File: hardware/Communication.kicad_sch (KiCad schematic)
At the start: 28 parts, among them J16 Conn_01x04_Pin, J17 Conn_01x03_Male, J18 USB_C_Receptacle_USB2.0, U31 TXB0102DCT, U32 ADUM4160

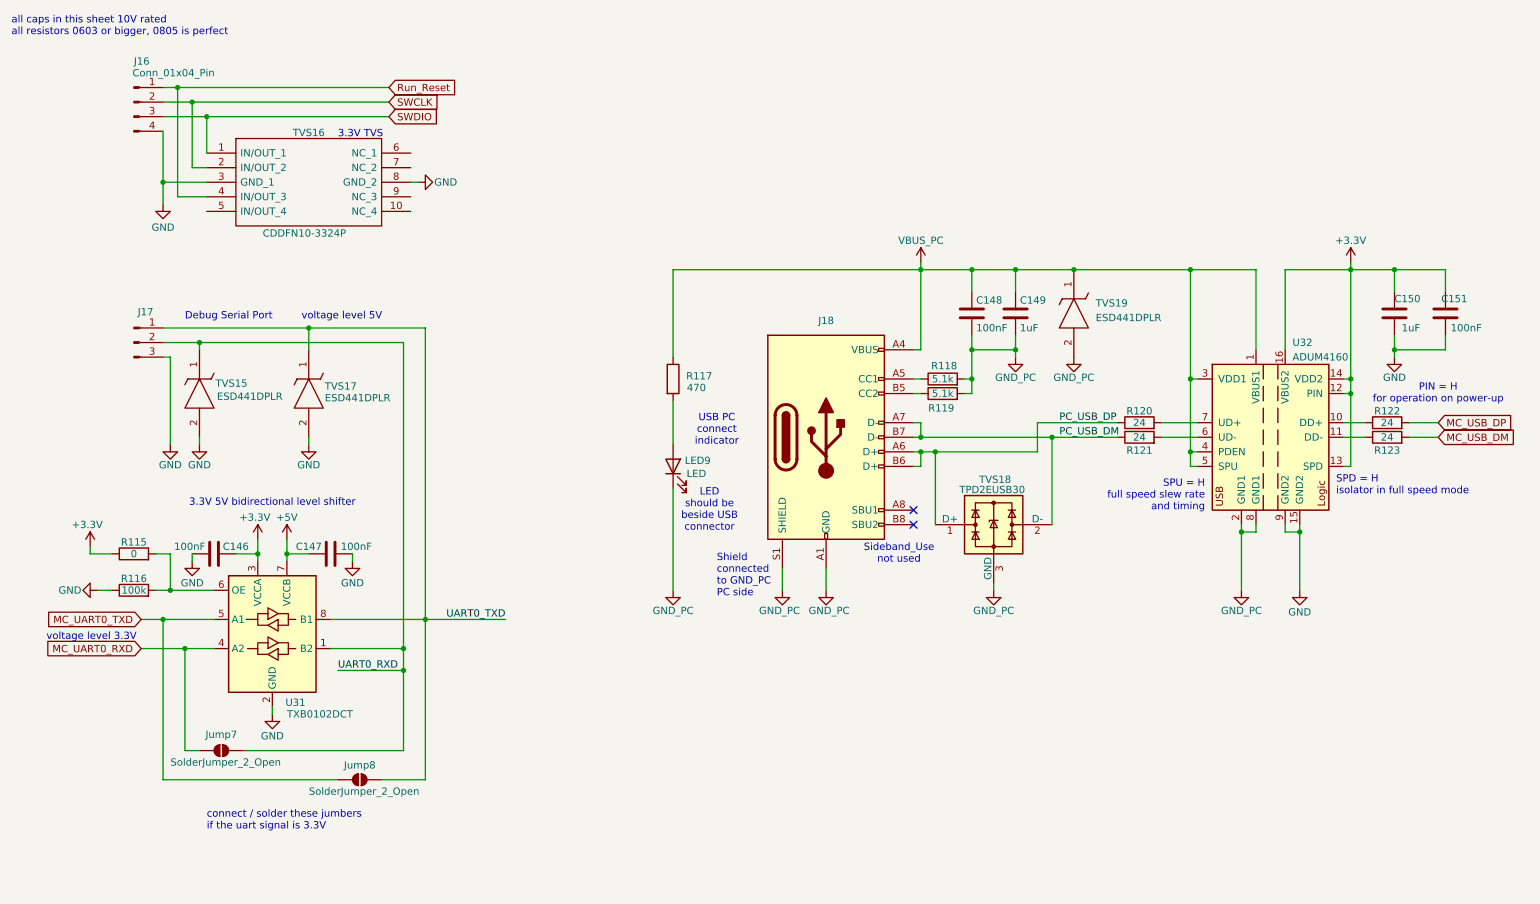
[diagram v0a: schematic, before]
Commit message: Added caps voltage rating + block diagram
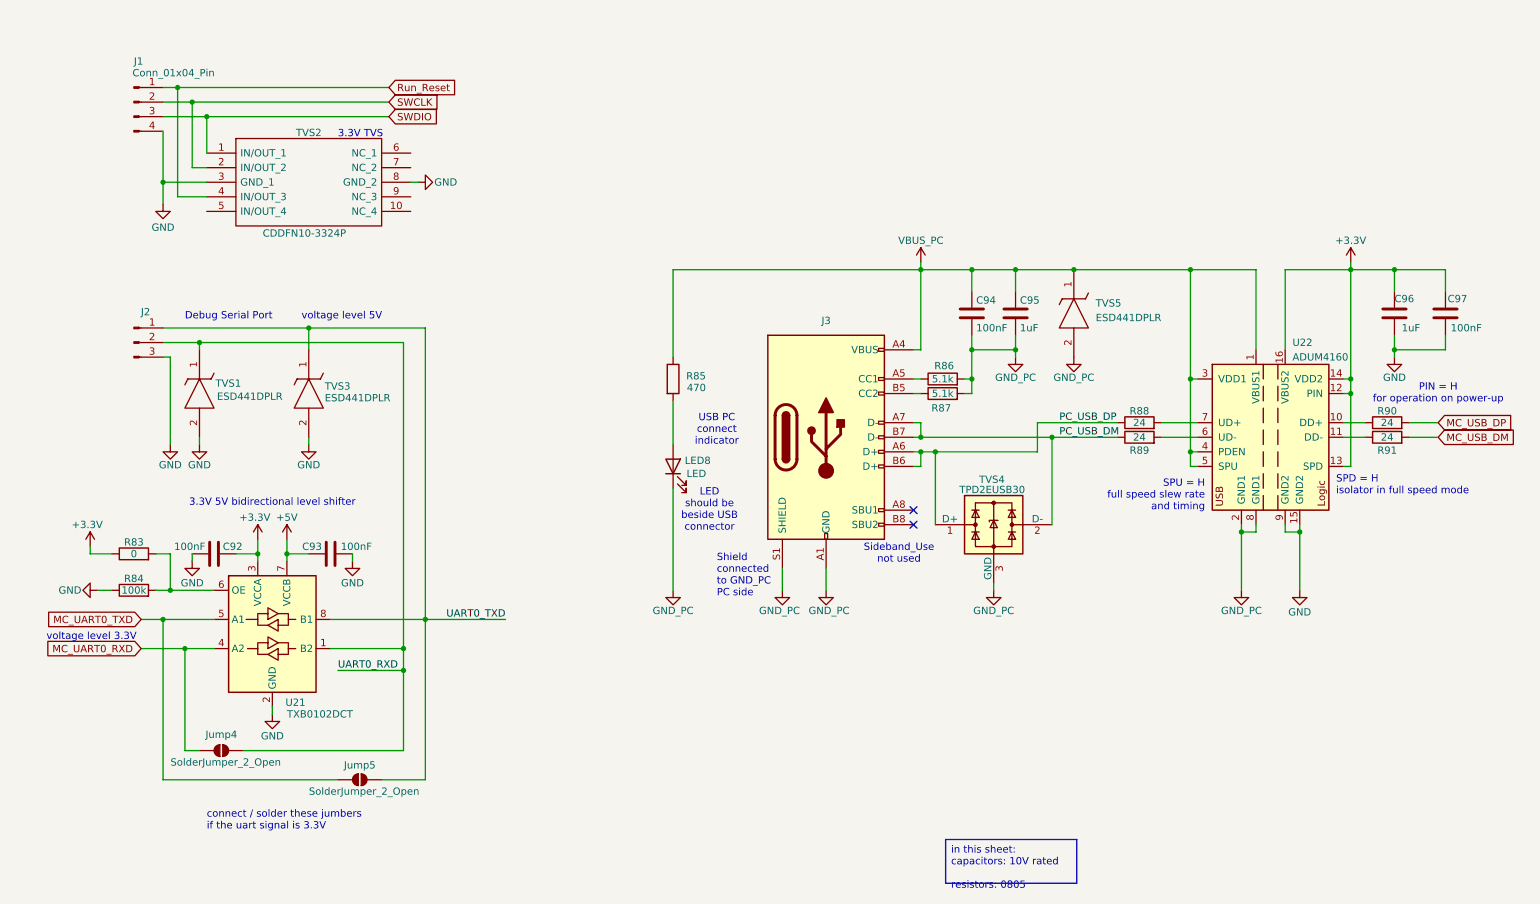
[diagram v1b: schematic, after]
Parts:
- renumbered C146 to C92, C147 to C93, C148 to C94, C149 to C95, C150 to C96, C151 to C97, J16 to J1, J17 to J2, J18 to J3, Jump7 to Jump4, Jump8 to Jump5, LED9 to LED8, R115 to R83, R116 to R84, R117 to R85, R118 to R86, R119 to R87, R120 to R88, R121 to R89, R122 to R90, R123 to R91, TVS15 to TVS1, TVS16 to TVS2, TVS17 to TVS3, TVS18 to TVS4, TVS19 to TVS5, U31 to U21, U32 to U22
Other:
- note removed: "all caps in this sheet 10V rated all resistors 0603 or bigger, 0805 is perfect"
- title: Multi Channel HARP DAC -> harp device quad dac

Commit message: The footprint assigning and reviewing have started.
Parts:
- C92, C93, C94, C95, C96, C97: symbol Device:C -> harp.device.quad.dac:C
- J1: symbol Connector:Conn_01x04_Pin -> harp.device.quad.dac:Conn_01x04_Pin
- J2: symbol Connector:Conn_01x03_Male -> harp.device.quad.dac:Conn_01x03_Male
- J3: symbol Connector:USB_C_Receptacle_USB2.0 -> harp.device.quad.dac:USB_C_Receptacle_USB2.0
- Jump4, Jump5: symbol Jumper:SolderJumper_2_Open -> harp.device.quad.dac:SolderJumper_2_Open
- LED8: symbol Device:LED -> harp.device.quad.dac:LED
- R83, R84, R85, R86, R87, R88, R89, R90, R91: symbol Device:R -> harp.device.quad.dac:R
- TVS1, TVS3, TVS5: symbol ESD441DPLR:ESD441DPLR -> harp.device.quad.dac:ESD441DPLR
- TVS2: symbol CDDFN10-3324P:CDDFN10-3324P -> harp.device.quad.dac:CDDFN10-3324P
- TVS4: symbol Power_Protection:TPD2EUSB30 -> harp.device.quad.dac:TPD2EUSB30
- U21: symbol Logic_LevelTranslator:TXB0102DCT -> harp.device.quad.dac:TXB0102DCT
- U22: symbol Interface_USB:ADUM4160 -> harp.device.quad.dac:ADUM4160
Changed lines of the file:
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@@
 	)
 	(symbol
-		(lib_id "Device:R")
+		(lib_id "harp.device.quad.dac:R")
 		(at 176.53 80.01 90)
 		(unit 1)
@@
 	)
 	(symbol
-		(lib_id "Device:R")
+		(lib_id "harp.device.quad.dac:R")
 		(at 254 87.63 90)
 		(unit 1)
@@
 	)
 	(symbol
-		(lib_id "ESD441DPLR:ESD441DPLR")
+		(lib_id "harp.device.quad.dac:ESD441DPLR")
 		(at 46.99 72.39 270)
 		(unit 1)
@@
 	)
 	(symbol
-		(lib_id "Connector:Conn_01x04_Pin")
+		(lib_id "harp.device.quad.dac:Conn_01x04_Pin")
 		(at 35.56 29.21 0)
 		(unit 1)
@@
 	)
 	(symbol
-		(lib_id "ESD441DPLR:ESD441DPLR")
+		(lib_id "harp.device.quad.dac:ESD441DPLR")
 		(at 66.04 72.39 270)
 		(unit 1)
@@
 	)
 	(symbol
-		(lib_id "Jumper:SolderJumper_2_Open")
+		(lib_id "harp.device.quad.dac:SolderJumper_2_Open")
 		(at 74.93 147.32 0)
 		(unit 1)
@@
 	)
 	(symbol
-		(lib_id "Device:R")
+		(lib_id "harp.device.quad.dac:R")
 		(at 35.56 114.3 90)
 		(unit 1)
@@
 	)
 	(symbol
-		(lib_id "Device:C")
+		(lib_id "harp.device.quad.dac:C")
 		(at 49.53 107.95 270)
 		(unit 1)
@@
 	)
 	(symbol
-		(lib_id "Power_Protection:TPD2EUSB30")
+		(lib_id "harp.device.quad.dac:TPD2EUSB30")
 		(at 185.42 102.87 0)
 		(unit 1)
@@
 	)
 	(symbol
-		(lib_id "ESD441DPLR:ESD441DPLR")
+		(lib_id "harp.device.quad.dac:ESD441DPLR")
 		(at 199.39 58.42 270)
 		(unit 1)
@@
 	)
 	(symbol
-		(lib_id "Connector:Conn_01x03_Male")
+		(lib_id "harp.device.quad.dac:Conn_01x03_Male")
 		(at 35.56 71.12 0)
 		(unit 1)
@@
 	)
 	(symbol
-		(lib_id "Device:R")
+		(lib_id "harp.device.quad.dac:R")
 		(at 210.82 87.63 90)
 		(unit 1)
@@
 	)
 	(symbol
-		(lib_id "Device:R")
+		(lib_id "harp.device.quad.dac:R")
 		(at 176.53 77.47 90)
 		(unit 1)
@@
 	)
 	(symbol
-		(lib_id "Logic_LevelTranslator:TXB0102DCT")
+		(lib_id "harp.device.quad.dac:TXB0102DCT")
 		(at 59.69 121.92 0)
 		(unit 1)
@@
 	)
 	(symbol
-		(lib_id "Connector:USB_C_Receptacle_USB2.0")
+		(lib_id "harp.device.quad.dac:USB_C_Receptacle_USB2.0")
 		(at 156.21 87.63 0)
 		(unit 1)
@@
 	)
 	(symbol
-		(lib_id "Device:R")
+		(lib_id "harp.device.quad.dac:R")
 		(at 35.56 107.95 90)
 		(unit 1)
@@
 	)
 	(symbol
-		(lib_id "Jumper:SolderJumper_2_Open")
+		(lib_id "harp.device.quad.dac:SolderJumper_2_Open")
 		(at 50.8 142.24 0)
 		(unit 1)
@@
 	)
 	(symbol
-		(lib_id "Device:C")
+		(lib_id "harp.device.quad.dac:C")
 		(at 264.16 66.04 180)
 		(unit 1)
@@
 	)
 	(symbol
-		(lib_id "Device:R")
+		(lib_id "harp.device.quad.dac:R")
 		(at 254 85.09 90)
 		(unit 1)
@@
 	)
 	(symbol
-		(lib_id "Device:R")
+		(lib_id "harp.device.quad.dac:R")
 		(at 129.54 77.47 0)
 		(unit 1)
@@
 	)
 	(symbol
-		(lib_id "Device:C")
+		(lib_id "harp.device.quad.dac:C")
 		(at 255.27 66.04 0)
 		(unit 1)
@@
 	)
 	(symbol
-		(lib_id "Device:R")
+		(lib_id "harp.device.quad.dac:R")
 		(at 210.82 85.09 90)
 		(unit 1)
@@
 	)
 	(symbol
-		(lib_id "Interface_USB:ADUM4160")
+		(lib_id "harp.device.quad.dac:ADUM4160")
 		(at 233.68 87.63 0)
 		(unit 1)
@@
 	)
 	(symbol
-		(lib_id "Device:C")
+		(lib_id "harp.device.quad.dac:C")
 		(at 181.61 66.04 180)
 		(unit 1)
@@
 	)
 	(symbol
-		(lib_id "Device:LED")
+		(lib_id "harp.device.quad.dac:LED")
 		(at 129.54 92.71 90)
 		(unit 1)
@@
 	)
 	(symbol
-		(lib_id "Device:C")
+		(lib_id "harp.device.quad.dac:C")
 		(at 189.23 66.04 0)
 		(unit 1)
@@
 	)
 	(symbol
-		(lib_id "Device:C")
+		(lib_id "harp.device.quad.dac:C")
 		(at 69.85 107.95 270)
 		(unit 1)
@@
 	)
 	(symbol
-		(lib_id "CDDFN10-3324P:CDDFN10-3324P")
+		(lib_id "harp.device.quad.dac:CDDFN10-3324P")
 		(at 48.26 38.1 0)
 		(unit 1)

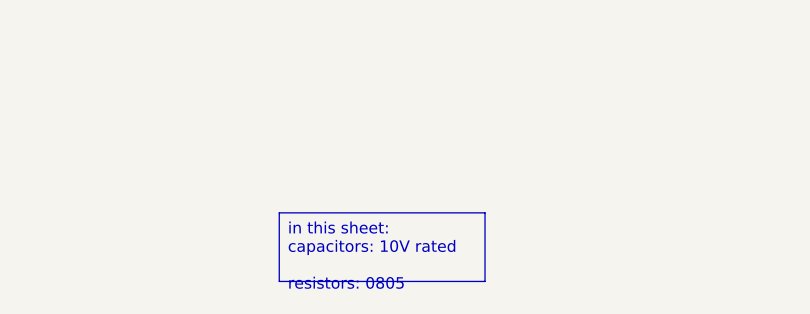
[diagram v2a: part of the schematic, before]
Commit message: Modified notes about caps and resistors
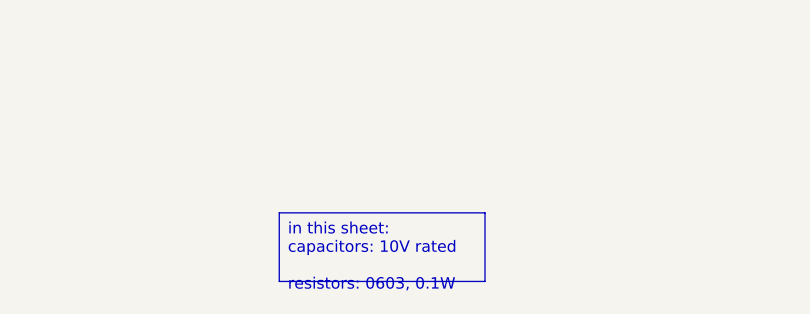
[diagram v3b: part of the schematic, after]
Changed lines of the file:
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@@
 		)
 	)
-	(text_box "in this sheet:\ncapacitors: 10V rated \nresistors: 0805"
+	(text_box "in this sheet:\ncapacitors: 10V rated \nresistors: 0603, 0.1W"
 		(exclude_from_sim no)
 		(at 177.038 157.734 0)

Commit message: Updating some footprints
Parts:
- C92, C93, C94, C95, C96, C97: footprint Capacitor_SMD:C_0402_1005Metric -> Capacitor_SMD:C_0603_1608Metric; symbol harp.device.quad.dac:C -> harp.device.quad.dac:C_0603
- Jump4, Jump5: footprint (none) -> harp.device.quad.dac.kicad:R_0603_1608Metric_Pad0.98x0.95mm_HandSolder
- LED8: footprint LED_SMD:LED_0603_1608Metric_Pad1.05x0.95mm_HandSolder -> harp.device.quad.dac.kicad:LED_0603_1608Metric_Pad1.05x0.95mm_HandSolder; MFN (none) -> SunLED; MPN (none) -> XZCDGK53W-1VF
- R83, R84, R85, R86, R87, R88, R89, R90, R91: footprint Resistor_SMD:R_0402_1005Metric -> Resistor_SMD:R_0603_1608Metric; symbol harp.device.quad.dac:R -> harp.device.quad.dac:R_0603

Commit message: The layout design has begun.
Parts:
- added J22, J23: Conn_01x02, Connector_PinHeader_2.54mm:PinHeader_1x02_P2.54mm_Vertical, symbol harp.device.quad.dac:Conn_01x02
- J1: footprint (none) -> Connector_PinHeader_2.54mm:PinHeader_1x04_P2.54mm_Vertical
- J2: footprint Connector_PinHeader_2.54mm:PinHeader_1x03_P2.54mm_Vertical -> harp.device.quad.dac.kicad:PinHeader_1x03_P2.54mm_Vertical
- J3: footprint Connector_USB:USB_C_Receptacle_JAE_DX07S016JA1R1500 -> harp.device.quad.dac.kicad:USB_C_Receptacle_JAE_DX07S016JA1R1500
- TVS1, TVS3, TVS5: footprint ESD441DPLR -> harp.device.quad.dac.kicad:ESD441DPLR
- U21: footprint Package_SO:TSSOP-8_3x3mm_P0.65mm -> harp.device.quad.dac.kicad:SOP50P310X90-8N
- U22: footprint Package_SO:SOIC-16W_7.5x10.3mm_P1.27mm -> harp.device.quad.dac.kicad:SOIC-16W_7.5x10.3mm_P1.27mm
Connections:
- net MC_UART0_RXD: now also J22.1 (Pin_1)
- net MC_UART0_TXD: now also J23.2 (Pin_2)
- net UART0_RXD: now also J22.2 (Pin_2)
- net UART0_TXD: now also J23.1 (Pin_1)
- no-connect marks 2 -> 7

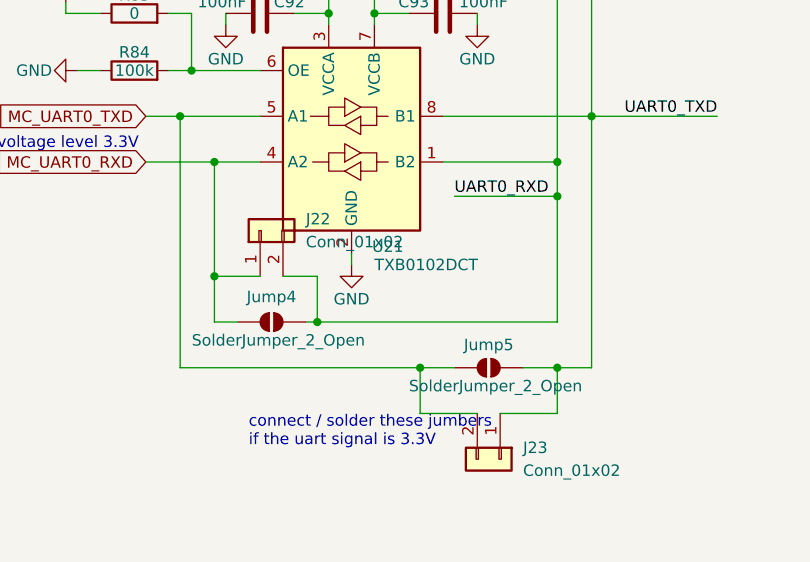
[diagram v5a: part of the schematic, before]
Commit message: Jumpers and interstages connections + added zeners to supply sections + justified text
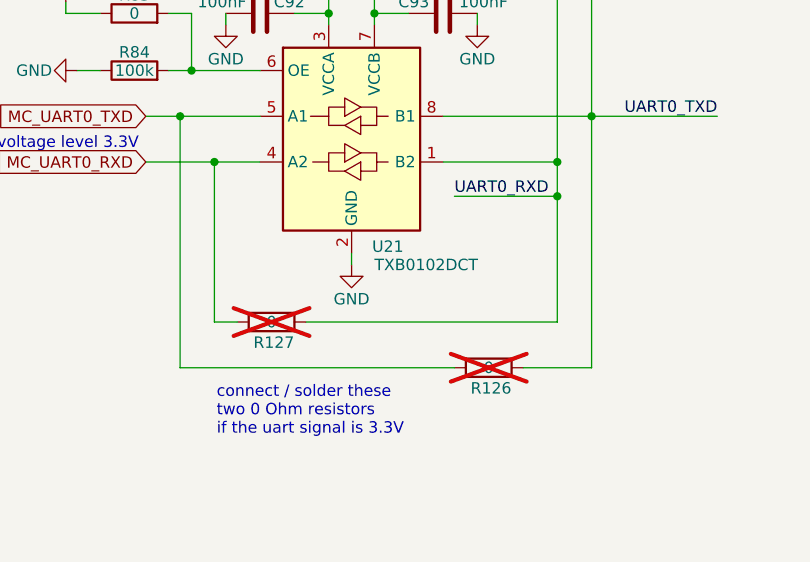
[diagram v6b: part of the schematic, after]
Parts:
- removed J22, J23: Conn_01x02, Connector_PinHeader_2.54mm:PinHeader_1x02_P2.54mm_Vertical, symbol harp.device.quad.dac:Conn_01x02
- removed Jump4, Jump5: SolderJumper_2_Open, harp.device.quad.dac.kicad:R_0603_1608Metric_Pad0.98x0.95mm_HandSolder, symbol harp.device.quad.dac:SolderJumper_2_Open
- added R126, R127: 0, Resistor_SMD:R_0603_1608Metric, symbol harp.device.quad.dac:R_0603
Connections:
- net MC_UART0_RXD: now also R127.1
- net MC_UART0_TXD: now also R126.1
- net UART0_RXD: now also R127.2
- net UART0_TXD: now also R126.2
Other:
- note added: "connect / solder these two 0 Ohm resistors if the uart signal is 3.3V"
- note removed: "connect / solder these jumbers if the uart signal is 3.3V"
